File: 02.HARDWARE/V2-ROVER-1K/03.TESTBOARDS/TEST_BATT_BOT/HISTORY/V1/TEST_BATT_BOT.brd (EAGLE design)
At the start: 18 x 18 mm, 6 parts

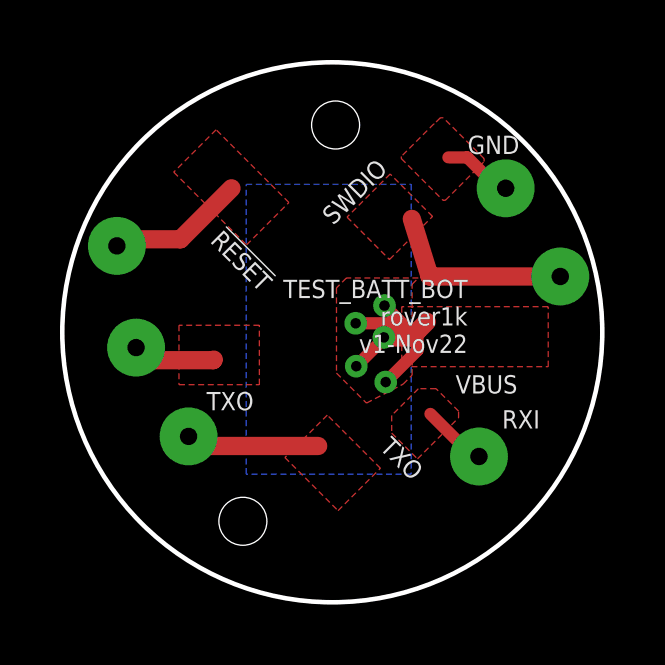
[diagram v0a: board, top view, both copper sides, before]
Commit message: Pedido PCBWAY compatible con v2 de PCB CONN
PCB CONN ha movido los testpoints y se añade RXI
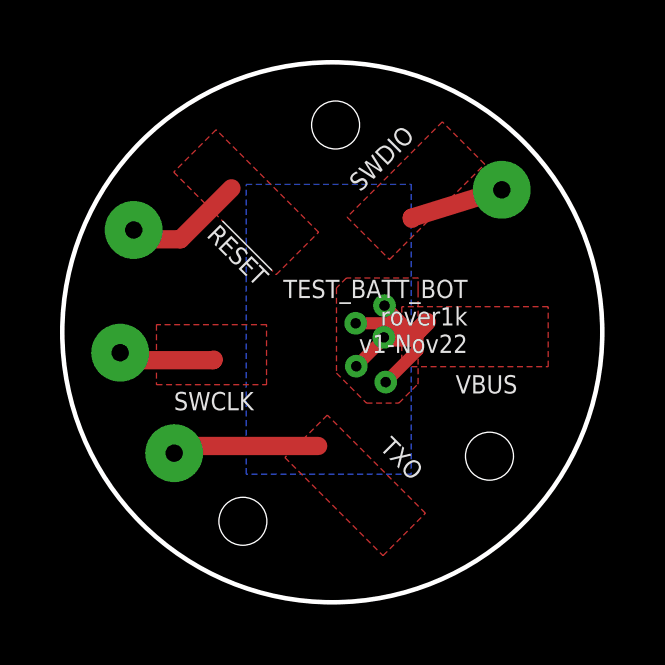
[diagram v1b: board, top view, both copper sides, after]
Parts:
- removed GND, RXI: (no value), SparkFun-Connectors:1X01_POGOPIN_HOLE_0.061_DIA
- moved SWDIO 3.49 mm to (44.5, 43.7)
- moved !RESET 0.77 mm to (32.2, 42.3)
- moved TXO 0.74 mm to (33.6, 34.9)
- moved SWCLK 0.56 mm to (31.8, 38.2)
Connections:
- removed net GND: GND.2
- removed net RXI: RXI.2
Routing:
- net SWDIO: track 6.36 -> 3.18 mm
- net GND: track 2.34 -> 0.00 mm
- net RXI: track 2.21 -> 0.00 mm
- net !RESET: track 4.62 -> 4.09 mm
- removed copper zone on layer 1, net GND
- removed copper zone on layer 1, net RXI
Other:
- board text added: "SWCLK"
